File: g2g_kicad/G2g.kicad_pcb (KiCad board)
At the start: 2 copper layers, 12 parts, among them U1 NANOPI, U2 mux

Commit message: Increase heiht
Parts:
- moved SOCKET_LOW1 12.7 mm to (40.6, 114.3)
- moved U2 11.1 mm to (49.1, 106.8)
- moved IMU0 4.15 mm to (84.7, 110.2)
- moved IMU1 3.60 mm to (49.1, 85.7)
- moved IMU2 3.60 mm to (54.2, 85.7)
- moved IMU3 3.60 mm to (59.3, 85.7)
- moved IMU4 3.60 mm to (64.3, 85.7)
- moved IMU5 3.60 mm to (69.4, 85.7)
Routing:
- net Net-(IMU0-Pad2): track 82.7 -> 96.9 mm
- net Net-(IMU5-Pad3): track 37.0 -> 50.4 mm
- net Net-(IMU5-Pad4): track 31.9 -> 44.6 mm
- net Net-(IMU4-Pad3): track 33.7 -> 45.7 mm
- net Net-(IMU4-Pad4): track 29.1 -> 41.1 mm
- net Net-(IMU3-Pad3): track 31.3 -> 43.3 mm
- net Net-(IMU3-Pad4): track 26.7 -> 38.7 mm
- net Net-(IMU0-Pad1): track 77.7 -> 89.6 mm
- net Net-(IMU2-Pad3): track 29.9 -> 40.7 mm
- net Net-(IMU2-Pad4): track 24.8 -> 35.5 mm
- net Net-(IMU0-Pad4): track 29.8 -> 39.0 mm
- net Net-(IMU0-Pad3): track 41.8 -> 50.9 mm
- net Net-(IMU1-Pad4): track 22.8 -> 31.0 mm
- net Net-(IMU1-Pad3): track 28.8 -> 36.5 mm
- net Net-(OLED1-Pad1): track 114.6 -> 118.3 mm
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
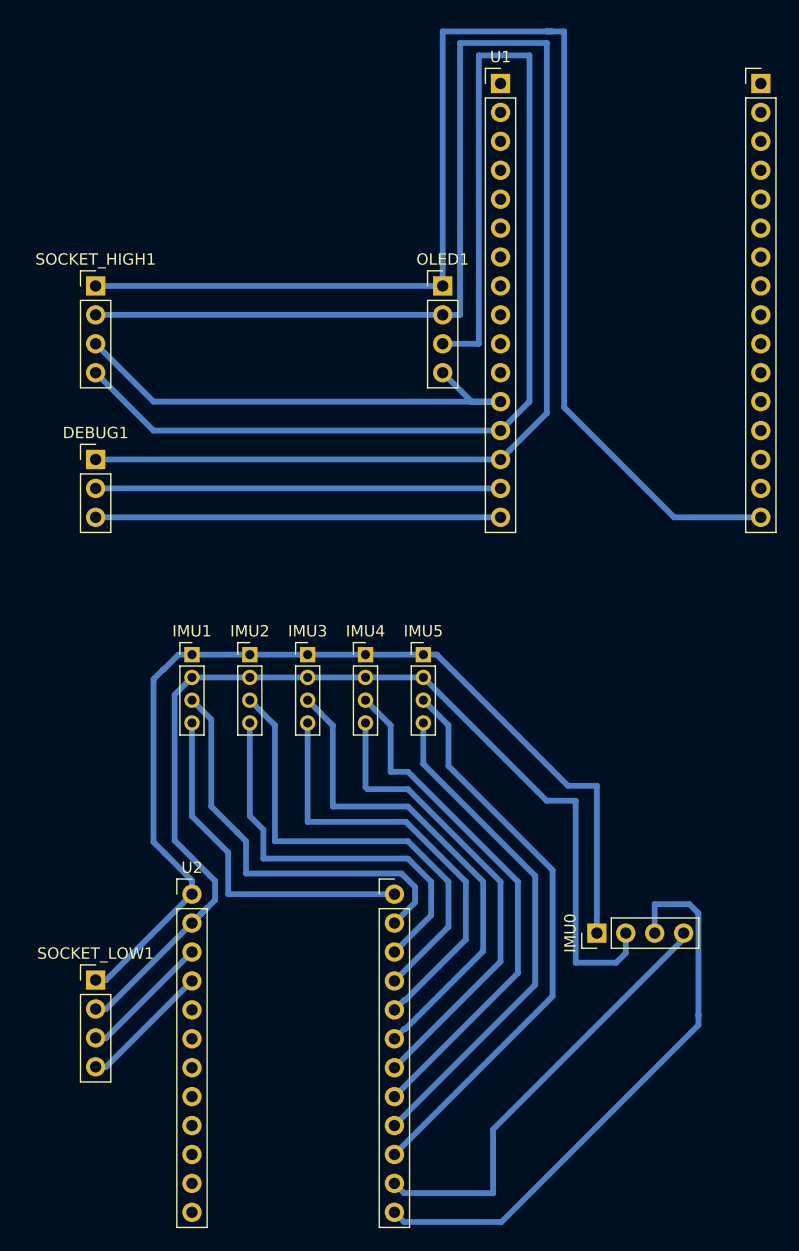
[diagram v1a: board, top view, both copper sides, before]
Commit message: Add Nut bolt holes
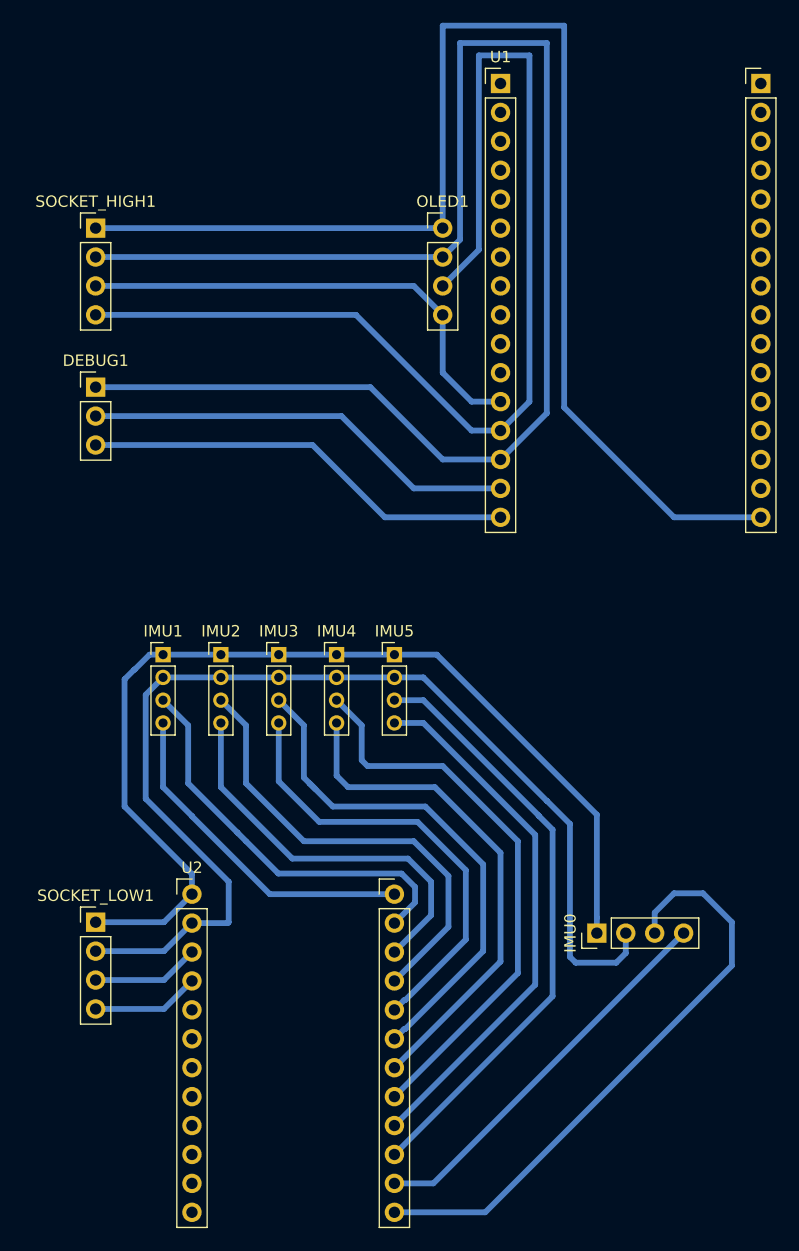
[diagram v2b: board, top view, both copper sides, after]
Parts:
- moved DEBUG1 6.35 mm to (40.6, 62.2)
- moved OLED1 5.08 mm to (71.1, 48.3)
- moved SOCKET_HIGH1 5.08 mm to (40.6, 48.3)
- moved SOCKET_LOW1 5.08 mm to (40.6, 109.2)
- moved IMU1 2.54 mm to (46.6, 85.7)
- moved IMU2 2.54 mm to (51.6, 85.7)
- moved IMU3 2.54 mm to (56.7, 85.7)
- moved IMU4 2.54 mm to (61.8, 85.7)
- moved IMU5 2.54 mm to (66.9, 85.7)
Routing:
- net Net-(OLED1-Pad3): track 104.6 -> 99.8 mm
- net Net-(OLED1-Pad1): track 118.3 -> 113.7 mm
- net Net-(IMU0-Pad4): track 39.0 -> 34.5 mm
- net Net-(IMU4-Pad3): track 45.7 -> 49.8 mm
- net Net-(IMU4-Pad4): track 41.1 -> 44.6 mm
- net Net-(DEBUG1-Pad1): track 137.3 -> 134.0 mm
- net Net-(IMU3-Pad3): track 43.3 -> 45.9 mm
- net Net-(DEBUG1-Pad2): track 35.6 -> 38.2 mm
- net Net-(DEBUG1-Pad3): track 35.6 -> 38.2 mm
- net Net-(IMU5-Pad4): track 44.6 -> 47.1 mm
- net Net-(IMU5-Pad3): track 50.4 -> 52.9 mm
- net Net-(SOCKET_LOW1-Pad4): track 11.6 -> 9.59 mm
- net Net-(SOCKET_LOW1-Pad3): track 11.6 -> 9.70 mm
- net Net-(IMU0-Pad3): track 50.9 -> 52.8 mm
- net Net-(IMU0-Pad2): track 96.9 -> 98.1 mm
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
